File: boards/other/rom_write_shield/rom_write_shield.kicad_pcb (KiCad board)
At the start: 2 copper layers, 58.4 x 53.3 mm, 38 parts, among them J1 Conn_01x08, J2 Conn_01x06, J3 Conn_01x08, J4 Conn_01x06, J5 Conn_02x10_Top_Bottom, J6 Conn_01x02, J7 vraw_test, Q1 2SC1815, U1 LT1930, U2 LM358N

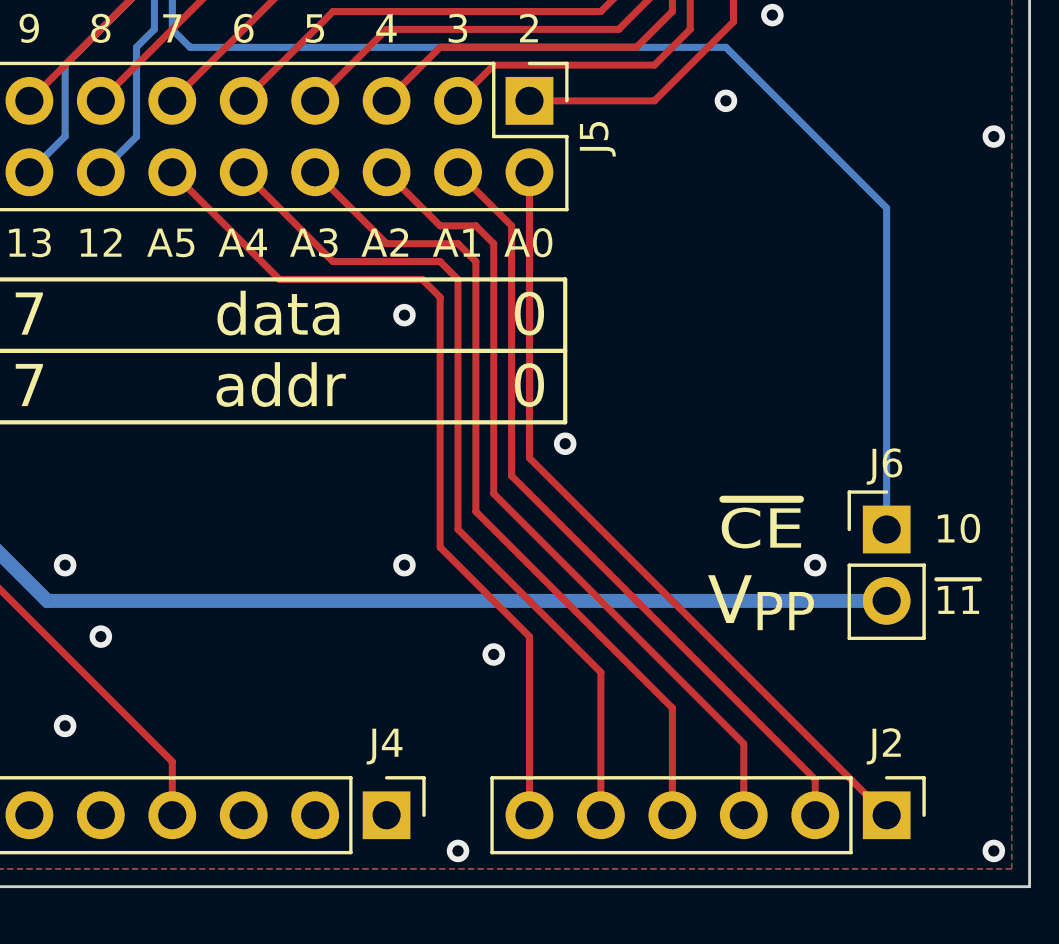
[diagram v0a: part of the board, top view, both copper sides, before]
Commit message: fix rom_write_shield and convenient_port_shield
fix reversed Arduino analog ports
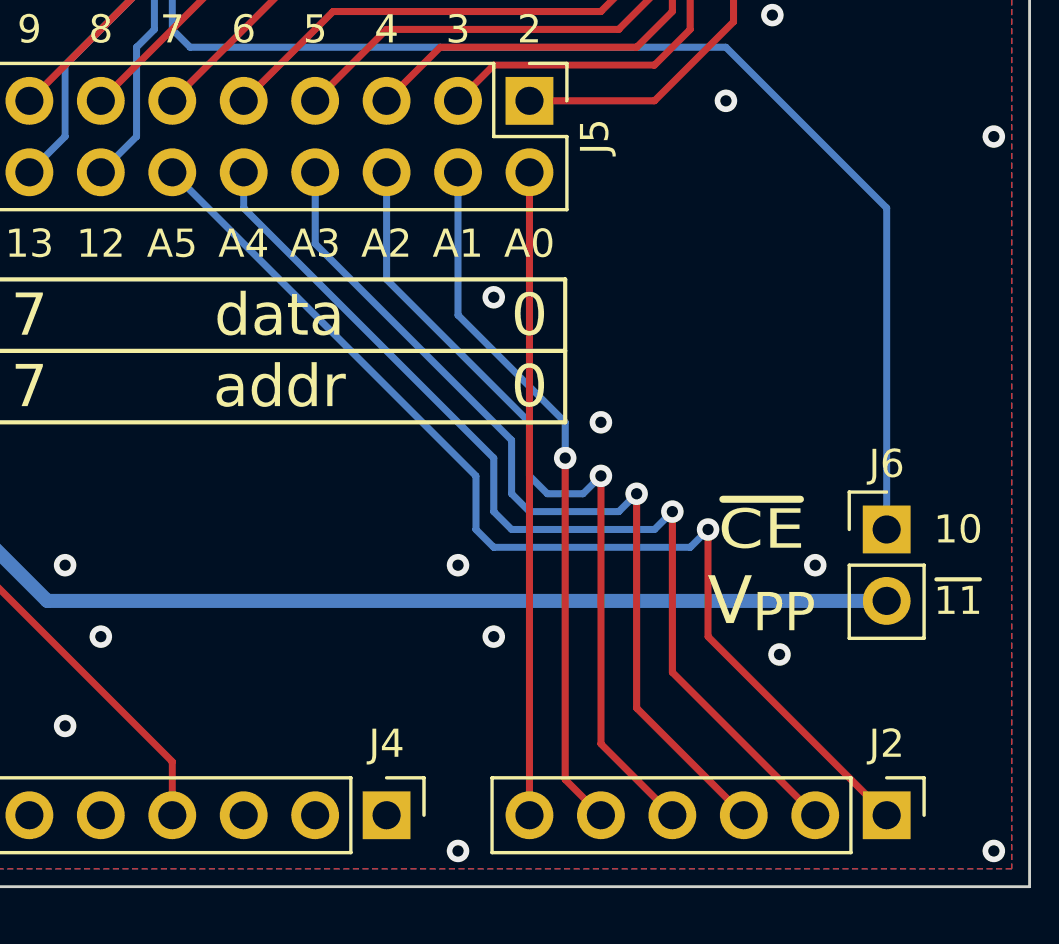
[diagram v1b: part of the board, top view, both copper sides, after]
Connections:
- J2 pad 1: /addr0 -> /addr5
- J2 pad 2: /addr1 -> /addr4
- J2 pad 3: /addr2 -> /addr3
- J2 pad 4: /addr3 -> /addr2
- J2 pad 5: /addr4 -> /addr1
- J2 pad 6: /addr5 -> /addr0
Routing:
- net /addr5: track 31.1 -> 38.7 mm, vias 0 -> 1
- net /addr0: track 28.1 -> 22.9 mm
- net /addr4: track 30.4 -> 35.5 mm, vias 0 -> 1
- net /addr1: track 28.1 -> 25.0 mm, vias 0 -> 1
- net /addr3: track 29.6 -> 32.3 mm, vias 0 -> 1
- net /addr2: track 28.9 -> 29.1 mm, vias 0 -> 1
- net GND: vias 36 -> 37
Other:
- board text added: "EPROM Programming Shield v1.1"
- board text removed: "EPROM Programming Shield v1.0"
